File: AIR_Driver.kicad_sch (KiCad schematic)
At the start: 6 parts, among them J8 MolexMicrofitPlus, Q3 DMN61D8LQ, Q4 DMN61D8LQ

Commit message: schematic: Do some general tidying
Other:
- note removed: "+"
- note removed: "-"
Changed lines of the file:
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@@
-		)
-	)
-	(text "+"
-		(exclude_from_sim no)
-		(at 167.132 94.742 0)
-		(effects
-			(font
-				(size 1.27 1.27)
-			)
-		)
-	)
-	(text "-"
-		(exclude_from_sim no)
-		(at 169.672 87.122 0)
-		(effects
-			(font
-				(size 1.27 1.27)
-			)
 		)
 	)

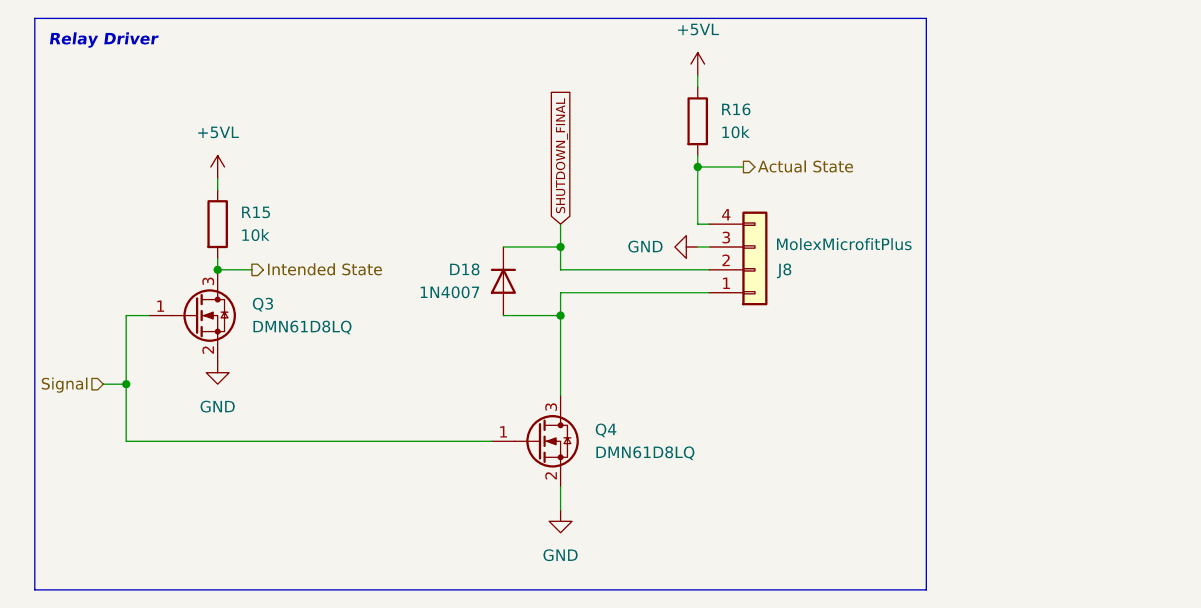
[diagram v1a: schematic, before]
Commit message: schematic: Mark AIR flyback diodes as DNP
The contactors should have them built-in.
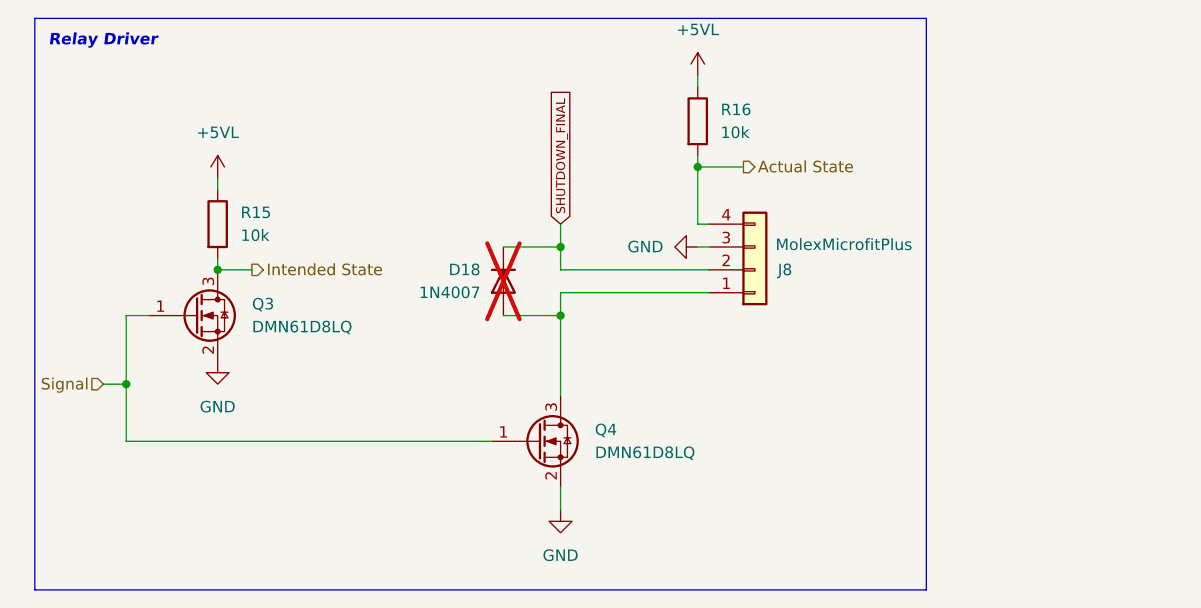
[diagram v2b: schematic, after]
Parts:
- D18: now not fitted
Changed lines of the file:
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@@
 		(on_board yes)
 		(dnp no)
-		(fields_autoplaced yes)
 		(property "Reference" "#PWR048"
 			(at 116.84 60.96 0)
@@
 		(in_bom yes)
 		(on_board yes)
-		(dnp no)
+		(dnp yes)
 		(property "Reference" "D18"
 			(at 92.71 78.7399 90)

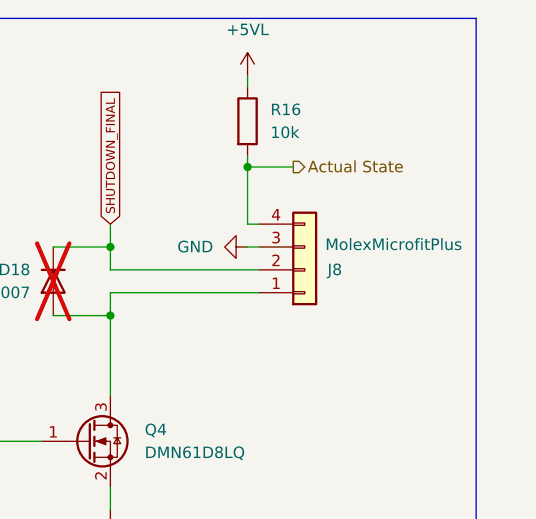
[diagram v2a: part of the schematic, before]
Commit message: schematic: Update molex connectors
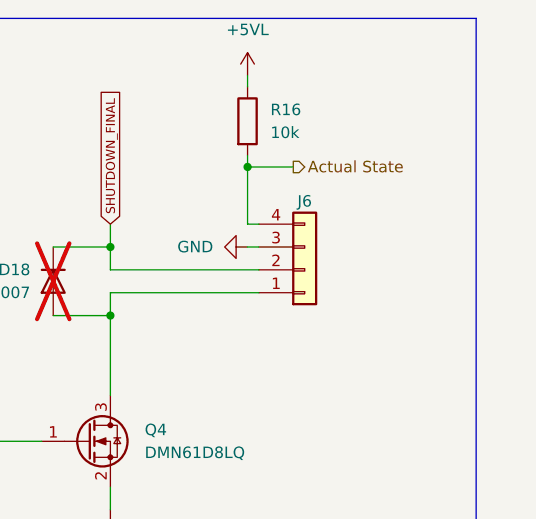
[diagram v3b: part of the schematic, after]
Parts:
- removed J8: MolexMicrofitPlus, symbol Connector_Generic:Conn_01x04
- added J6: Conn_01x04, yfs:MolexMicrofitPlus1x4, symbol Connector_Generic:Conn_01x04
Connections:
- net Actual State: now also J6.4 (Pin_4)
- net GND: now also J6.3 (Pin_3)
- net SHUTDOWN_FINAL: now also J6.2 (Pin_2)
- net at D18.2 (A), Q4.3 (D): now also J6.1 (Pin_1)
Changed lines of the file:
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@@
+	)
+	(symbol
+		(lib_id "Connector_Generic:Conn_01x04")
+		(at 123.19 78.74 0)
+		(mirror x)
+		(unit 1)
+		(exclude_from_sim no)
+		(in_bom yes)
+		(on_board yes)
+		(dnp no)
+		(property "Reference" "J6"
+			(at 123.19 71.12 0)
+			(effects
+				(font
+					(size 1.27 1.27)
+				)
+			)
+		)
+		(property "Value" "Conn_01x04"
+			(at 123.19 69.85 0)
+			(effects
+				(font
+					(size 1.27 1.27)
+				)
+				(hide yes)
+			)
+		)
+		(property "Footprint" "yfs:MolexMicrofitPlus1x4"
+			(at 123.19 78.74 0)
+			(effects
+				(font
+					(size 1.27 1.27)
+				)
+				(hide yes)
+			)
+		)
+		(property "Datasheet" "~"
+			(at 123.19 78.74 0)
+			(effects
+				(font
+					(size 1.27 1.27)
+				)
+				(hide yes)
+			)
+		)
+		(property "Description" "Generic connector, single row, 01x04, script generated (kicad-library-utils/schlib/autogen/connector/)"
+			(at 123.19 78.74 0)
+			(effects
+				(font
+					(size 1.27 1.27)
+				)
+				(hide yes)
+			)
+		)
+		(property "Dist" "Mouser"
+			(at 123.19 78.74 0)
+			(effects
+				(font
+					(size 1.27 1.27)
+				)
+				(hide yes)
+			)
+		)
+		(property "Dist #" "538-215760-1004"
+			(at 123.19 78.74 0)
+			(effects
+				(font
+					(size 1.27 1.27)
+				)
+				(hide yes)
+			)
+		)
+		(property "Mfr" "Molex"
+			(at 123.19 78.74 0)
+			(effects
+				(font
+					(size 1.27 1.27)
+				)
+				(hide yes)
+			)
+		)
+		(property "Mfr #" "2157601004"
+			(at 123.19 78.74 0)
+			(effects
+				(font
+					(size 1.27 1.27)
+				)
+				(hide yes)
+			)
+		)
+		(pin "4"
+		)
+		(pin "3"
+		)
+		(pin "2"
+		)
+		(pin "1"
+		)
+		(instances
+			(project "Precharge_PCB"
+				(path "/c467677d-b98c-4488-bd11-965ef67263b2/002009e0-fc6e-484e-9acf-1c1ff1f04f91"
+					(reference "J11")
+					(unit 1)
+				)
+				(path "/c467677d-b98c-4488-bd11-965ef67263b2/25042107-483b-420f-bbcd-e84a850709aa"
+					(reference "J6")
+					(unit 1)
+				)
+			)
+		)
 	)
 	(symbol
@@
 					(unit 1)
 				)
-			)
-		)
-	)
-	(symbol
-		(lib_id "Connector_Generic:Conn_01x04")
-		(at 123.19 78.74 0)
-		(mirror x)
-		(unit 1)
-		(exclude_from_sim no)
-		(in_bom yes)
-		(on_board yes)
-		(dnp no)
-		(property "Reference" "J8"
-			(at 125.73 78.7401 0)
-			(effects
-				(font
-					(size 1.27 1.27)
-				)
-				(justify left)
-			)
-		)
-		(property "Value" "MolexMicrofitPlus"
-			(at 125.476 75.946 0)
-			(effects
-				(font
-					(size 1.27 1.27)
-				)
-				(justify left)
-			)
-		)
-		(property "Footprint" ""
-			(at 123.19 78.74 0)
-			(effects
-				(font
-					(size 1.27 1.27)
-				)
-				(hide yes)
-			)
-		)
-		(property "Datasheet" "~"
-			(at 123.19 78.74 0)
-			(effects
-				(font
-					(size 1.27 1.27)
-				)
-				(hide yes)
-			)
-		)
-		(property "Description" "Generic connector, single row, 01x04, script generated (kicad-library-utils/schlib/autogen/connector/)"
-			(at 123.19 78.74 0)
-			(effects
-				(font
-					(size 1.27 1.27)
-				)
-				(hide yes)
-			)
-		)
-		(pin "1"
-		)
-		(pin "3"
-		)
-		(pin "2"
-		)
-		(pin "4"
-		)
-		(instances
-			(project "Precharge_PCB"
-				(path "/c467677d-b98c-4488-bd11-965ef67263b2/002009e0-fc6e-484e-9acf-1c1ff1f04f91"
-					(reference "J7")
-					(unit 1)
-				)
-				(path "/c467677d-b98c-4488-bd11-965ef67263b2/25042107-483b-420f-bbcd-e84a850709aa"
-					(reference "J8")
-					(unit 1)
-				)

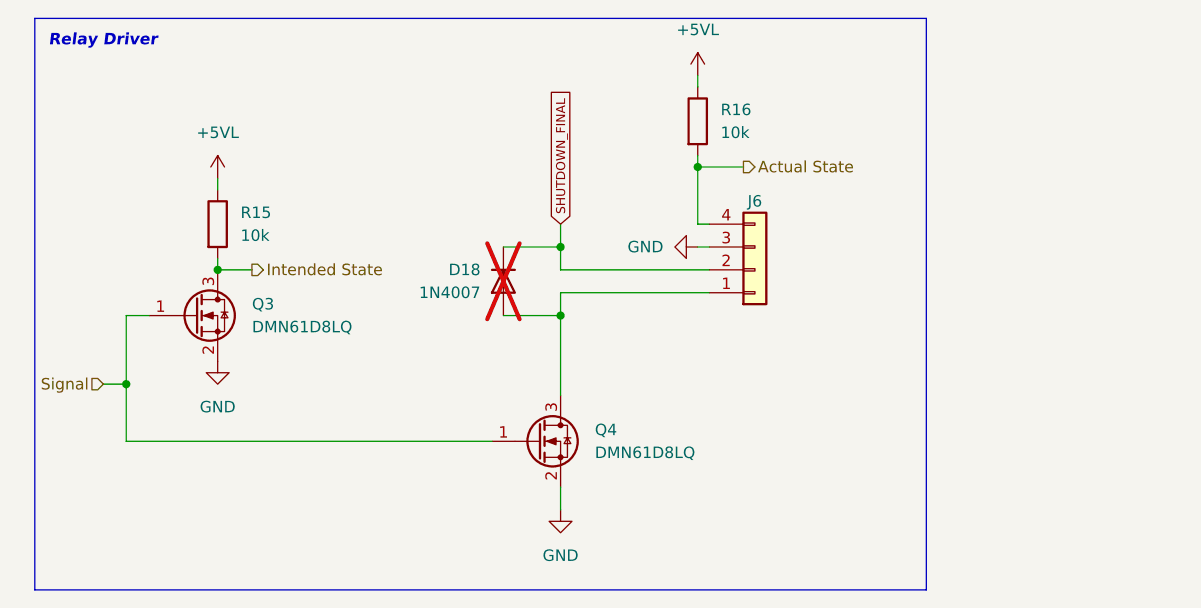
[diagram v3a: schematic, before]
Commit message: schematic: Reassign reference designators
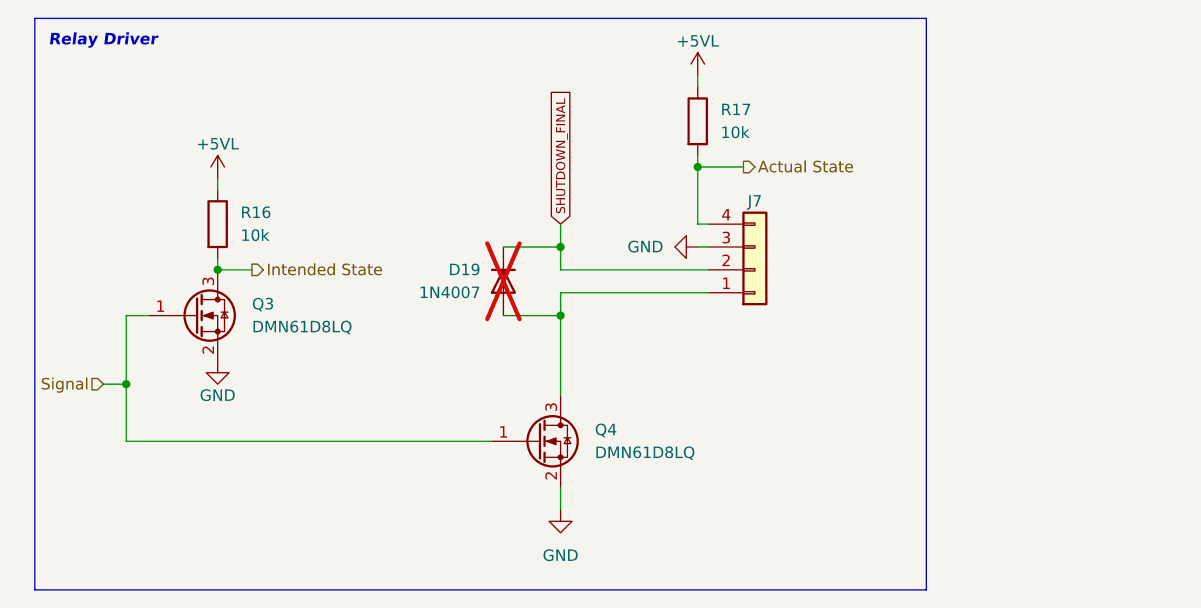
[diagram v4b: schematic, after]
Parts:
- renumbered D18 to D19, J6 to J7, R15 to R16, R16 to R17
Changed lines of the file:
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@@
 		(on_board yes)
 		(dnp no)
-		(property "Reference" "J6"
+		(property "Reference" "J7"
 			(at 123.19 71.12 0)
 			(effects
@@
 			(project "Precharge_PCB"
 				(path "/c467677d-b98c-4488-bd11-965ef67263b2/002009e0-fc6e-484e-9acf-1c1ff1f04f91"
-					(reference "J11")
-					(unit 1)
-				)
-				(path "/c467677d-b98c-4488-bd11-965ef67263b2/25042107-483b-420f-bbcd-e84a850709aa"
-					(reference "J6")
+					(reference "J8")
+					(unit 1)
+				)
+				(path "/c467677d-b98c-4488-bd11-965ef67263b2/25042107-483b-420f-bbcd-e84a850709aa"
+					(reference "J7")
 					(unit 1)
 				)
@@
 		(on_board yes)
 		(dnp no)
-		(fields_autoplaced yes)
 		(property "Reference" "#PWR045"
 			(at 63.5 72.39 0)
@@
 		)
 		(property "Value" "+5VL"
-			(at 63.5 63.5 0)
+			(at 63.5 64.77 0)
 			(effects
 				(font
@@
 		)
 		(property "Value" "+5VL"
-			(at 116.84 52.07 0)
+			(at 116.84 53.34 0)
 			(effects
 				(font
@@
 		(dnp no)
 		(fields_autoplaced yes)
-		(property "Reference" "R16"
+		(property "Reference" "R17"
 			(at 119.38 60.9599 0)
 			(effects
@@
 			(project "Precharge_PCB"
 				(path "/c467677d-b98c-4488-bd11-965ef67263b2/002009e0-fc6e-484e-9acf-1c1ff1f04f91"
-					(reference "R18")
-					(unit 1)
-				)
-				(path "/c467677d-b98c-4488-bd11-965ef67263b2/25042107-483b-420f-bbcd-e84a850709aa"
-					(reference "R16")
+					(reference "R19")
+					(unit 1)
+				)
+				(path "/c467677d-b98c-4488-bd11-965ef67263b2/25042107-483b-420f-bbcd-e84a850709aa"
+					(reference "R17")
 					(unit 1)
 				)
@@
 		(on_board yes)
 		(dnp no)
-		(fields_autoplaced yes)
 		(property "Reference" "#PWR046"
 			(at 63.5 95.25 0)
@@
 		)
 		(property "Value" "GND"
-			(at 63.5 93.98 0)
+			(at 63.5 92.71 0)
 			(effects
 				(font
@@
 		(dnp no)
 		(fields_autoplaced yes)
-		(property "Reference" "R15"
+		(property "Reference" "R16"
 			(at 66.04 72.3899 0)
 			(effects
@@
 			(project "Precharge_PCB"
 				(path "/c467677d-b98c-4488-bd11-965ef67263b2/002009e0-fc6e-484e-9acf-1c1ff1f04f91"
-					(reference "R17")
-					(unit 1)
-				)
-				(path "/c467677d-b98c-4488-bd11-965ef67263b2/25042107-483b-420f-bbcd-e84a850709aa"
-					(reference "R15")
+					(reference "R18")
+					(unit 1)
+				)
+				(path "/c467677d-b98c-4488-bd11-965ef67263b2/25042107-483b-420f-bbcd-e84a850709aa"
+					(reference "R16")
 					(unit 1)
 				)
@@
 		(on_board yes)
 		(dnp yes)
-		(property "Reference" "D18"
+		(property "Reference" "D19"
 			(at 92.71 78.7399 90)
 			(effects
@@
 			(project "Precharge_PCB"
 				(path "/c467677d-b98c-4488-bd11-965ef67263b2/002009e0-fc6e-484e-9acf-1c1ff1f04f91"
-					(reference "D17")
-					(unit 1)
-				)
-				(path "/c467677d-b98c-4488-bd11-965ef67263b2/25042107-483b-420f-bbcd-e84a850709aa"
-					(reference "D18")
-					(unit 1)
-				)
+					(reference "D20")
+					(unit 1)
+				)
+				(path "/c467677d-b98c-4488-bd11-965ef67263b2/25042107-483b-420f-bbcd-e84a850709aa"
+					(reference "D19")
+					(unit 1)
+				)

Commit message: schematic: Fill out most of the BOM
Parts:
- Q3, Q4: Dist (none) -> LCSC; Dist # (none) -> C5248874; Mfr (none) -> DIODES; Mfr # (none) -> DMN61D8LQ-7
- R16, R17: Dist (none) -> LCSC; Dist # (none) -> C25804; Mfr (none) -> Uni-Royal; Mfr # (none) -> 0603WAF1002T5E
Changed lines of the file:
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@@
+			)
+		)
+		(property "Dist" "LCSC"
+			(at 99.06 97.79 0)
+			(effects
+				(font
+					(size 1.27 1.27)
+				)
+				(hide yes)
+			)
+		)
+		(property "Dist #" "C5248874"
+			(at 99.06 97.79 0)
+			(effects
+				(font
+					(size 1.27 1.27)
+				)
+				(hide yes)
+			)
+		)
+		(property "Mfr" "DIODES"
+			(at 99.06 97.79 0)
+			(effects
+				(font
+					(size 1.27 1.27)
+				)
+				(hide yes)
+			)
+		)
+		(property "Mfr #" "DMN61D8LQ-7"
+			(at 99.06 97.79 0)
+			(effects
+				(font
+					(size 1.27 1.27)
+				)
+				(hide yes)
 			)
 		)
@@
 			)
 		)
+		(property "Dist" "LCSC"
+			(at 116.84 62.23 0)
+			(effects
+				(font
+					(size 1.27 1.27)
+				)
+				(hide yes)
+			)
+		)
+		(property "Dist #" "C25804"
+			(at 116.84 62.23 0)
+			(effects
+				(font
+					(size 1.27 1.27)
+				)
+				(hide yes)
+			)
+		)
+		(property "Mfr" "Uni-Royal"
+			(at 116.84 62.23 0)
+			(effects
+				(font
+					(size 1.27 1.27)
+				)
+				(hide yes)
+			)
+		)
+		(property "Mfr #" "0603WAF1002T5E"
+			(at 116.84 62.23 0)
+			(effects
+				(font
+					(size 1.27 1.27)
+				)
+				(hide yes)
+			)
+		)
 		(pin "1"
 		)
@@
 			)
 		)
+		(property "Dist" "LCSC"
+			(at 63.5 73.66 0)
+			(effects
+				(font
+					(size 1.27 1.27)
+				)
+				(hide yes)
+			)
+		)
+		(property "Dist #" "C25804"
+			(at 63.5 73.66 0)
+			(effects
+				(font
+					(size 1.27 1.27)
+				)
+				(hide yes)
+			)
+		)
+		(property "Mfr" "Uni-Royal"
+			(at 63.5 73.66 0)
+			(effects
+				(font
+					(size 1.27 1.27)
+				)
+				(hide yes)
+			)
+		)
+		(property "Mfr #" "0603WAF1002T5E"
+			(at 63.5 73.66 0)
+			(effects
+				(font
+					(size 1.27 1.27)
+				)
+				(hide yes)
+			)
+		)
 		(pin "1"
 		)
@@
 			(at 60.96 83.82 0)
 			(effects
+				(font
+					(size 1.27 1.27)
+				)
+				(hide yes)
+			)
+		)
+		(property "Dist" "LCSC"
+			(at 60.96 83.82 0)
+			(effects
+				(font
+					(size 1.27 1.27)
+				)
+				(hide yes)
+			)
+		)
+		(property "Dist #" "C5248874"
+			(at 60.96 83.82 0)
+			(effects
+				(font
+					(size 1.27 1.27)
+				)
+				(hide yes)
+			)
+		)
+		(property "Mfr" "DIODES"
+			(at 60.96 83.82 0)
+			(effects
+				(font
+					(size 1.27 1.27)
+				)
+				(hide yes)
+			)
+		)
+		(property "Mfr #" "DMN61D8LQ-7"
+			(at 60.96 83.82 0)
+			(effects

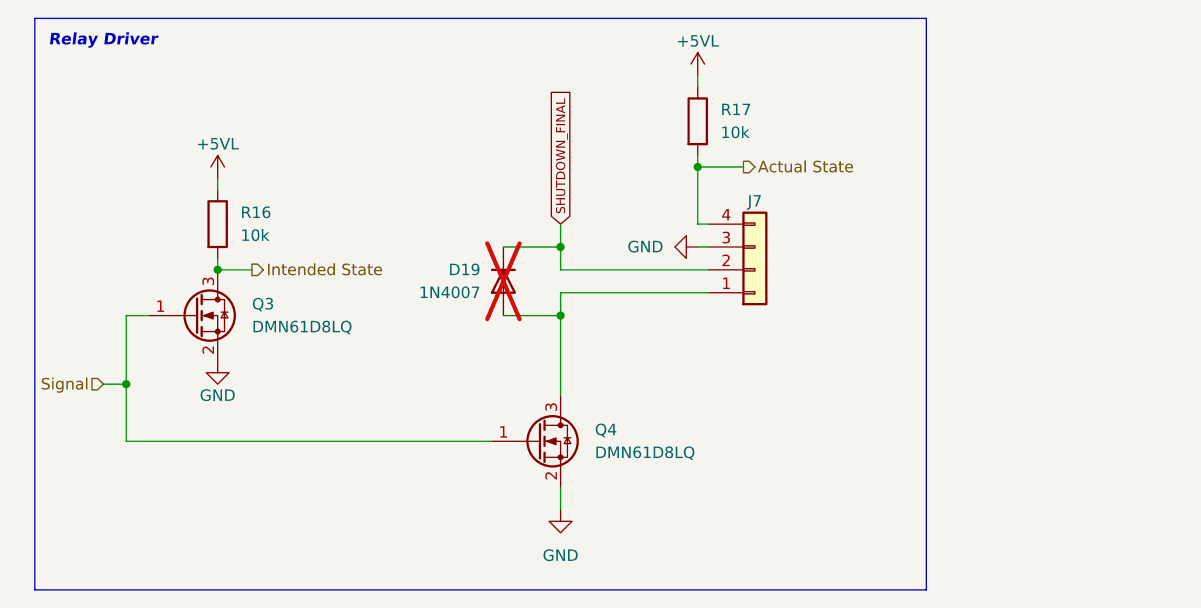
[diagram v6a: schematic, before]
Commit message: *: Remove AIR flyback diodes
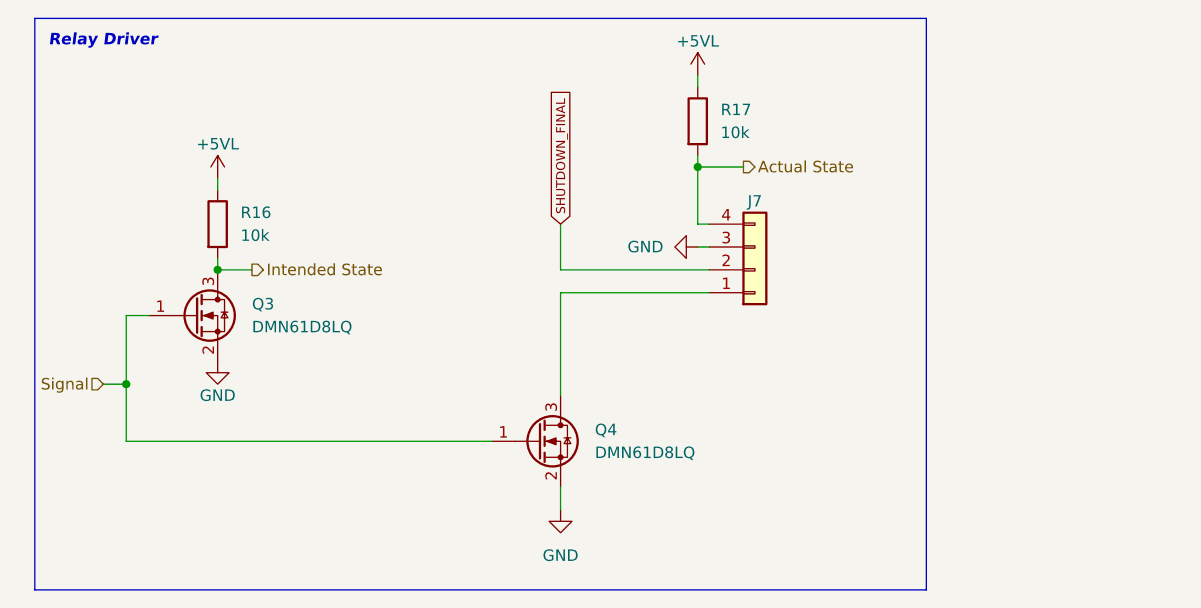
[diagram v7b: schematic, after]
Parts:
- removed D19: 1N4007, Diode_SMD:D_SMA, symbol Diode:1N4007
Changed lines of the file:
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@@
-	)
-	(junction
-		(at 101.6 83.82)
-		(diameter 0)
-		(color 0 0 0 0)
 	)
 	(junction
@@
 		(color 0 0 0 0)
 	)
-	(junction
-		(at 101.6 76.2)
-		(diameter 0)
-		(color 0 0 0 0)
-	)
 	(wire
 		(pts
@@
 	(wire
 		(pts
-			(xy 95.25 83.82) (xy 101.6 83.82)
-		)
-		(stroke
-			(width 0)
-			(type default)
-		)
-	)
-	(wire
-		(pts
 			(xy 50.8 91.44) (xy 53.34 91.44)
 		)
@@
 	(wire
 		(pts
-			(xy 95.25 76.2) (xy 101.6 76.2)
-		)
-		(stroke
-			(width 0)
-			(type default)
-		)
-	)
-	(wire
-		(pts
 			(xy 116.84 67.31) (xy 116.84 73.66)
 		)
@@
 	(wire
 		(pts
-			(xy 101.6 83.82) (xy 101.6 92.71)
-		)
-		(stroke
-			(width 0)
-			(type default)
-		)
-	)
-	(wire
-		(pts
-			(xy 101.6 81.28) (xy 101.6 83.82)
+			(xy 101.6 81.28) (xy 101.6 92.71)
 		)
 		(stroke
@@
 	(wire
 		(pts
-			(xy 101.6 73.66) (xy 101.6 76.2)
+			(xy 101.6 73.66) (xy 101.6 78.74)
 		)
 		(stroke
@@
 		(pts
 			(xy 53.34 91.44) (xy 53.34 97.79)
-		)
-		(stroke
-			(width 0)
-			(type default)
-		)
-	)
-	(wire
-		(pts
-			(xy 101.6 76.2) (xy 101.6 78.74)
 		)
 		(stroke
@@
 					(unit 1)
 				)
-			)
-		)
-	)
-	(symbol
-		(lib_id "Diode:1N4007")
-		(at 95.25 80.01 90)
-		(mirror x)
-		(unit 1)
-		(exclude_from_sim no)
-		(in_bom yes)
-		(on_board yes)
-		(dnp yes)
-		(property "Reference" "D19"
-			(at 92.71 78.7399 90)
-			(effects
-				(font
-					(size 1.27 1.27)
-				)
-				(justify left)
-			)
-		)
-		(property "Value" "1N4007"
-			(at 92.71 81.2799 90)
-			(effects
-				(font
-					(size 1.27 1.27)
-				)
-				(justify left)
-			)
-		)
-		(property "Footprint" "Diode_SMD:D_SMA"
-			(at 99.695 80.01 0)
-			(effects
-				(font
-					(size 1.27 1.27)
-				)
-				(hide yes)
-			)
-		)
-		(property "Datasheet" "http://www.vishay.com/docs/88503/1n4001.pdf"
-			(at 95.25 80.01 0)
-			(effects
-				(font
-					(size 1.27 1.27)
-				)
-				(hide yes)
-			)
-		)
-		(property "Description" "1000V 1A General Purpose Rectifier Diode, DO-41"
-			(at 95.25 80.01 0)
-			(effects
-				(font
-					(size 1.27 1.27)
-				)
-				(hide yes)
-			)
-		)
-		(property "Sim.Device" "D"
-			(at 95.25 80.01 0)
-			(effects
-				(font
-					(size 1.27 1.27)
-				)
-				(hide yes)
-			)
-		)
-		(property "Sim.Pins" "1=K 2=A"
-			(at 95.25 80.01 0)
-			(effects
-				(font
-					(size 1.27 1.27)
-				)
-				(hide yes)
-			)
-		)
-		(pin "2"
-		)
-		(pin "1"
-		)
-		(instances
-			(project "Precharge_PCB"
-				(path "/c467677d-b98c-4488-bd11-965ef67263b2/002009e0-fc6e-484e-9acf-1c1ff1f04f91"
-					(reference "D20")
-					(unit 1)
-				)
-				(path "/c467677d-b98c-4488-bd11-965ef67263b2/25042107-483b-420f-bbcd-e84a850709aa"
-					(reference "D19")
-					(unit 1)
-				)
